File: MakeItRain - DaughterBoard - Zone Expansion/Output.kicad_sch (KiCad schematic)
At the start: 8 parts, among them P4 Screw_Terminal_01x02, Q7 2N7000, Q8 IRF9Z34NPBF

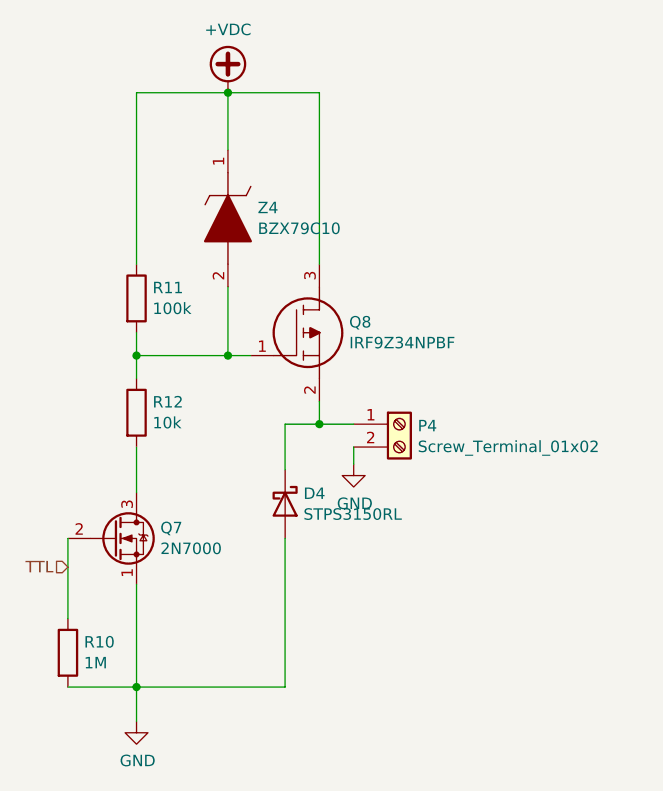
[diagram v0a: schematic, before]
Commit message: MakeItRain * Main Board Fixed Routing. * replaced Opamp with the part that i can get as the old one is EOL * generated all the fab files i need. * updated the daughter plug witht eh i2c ttl flip * fixed I2C issues * DRC'ed the board
MakeItRain - DaughterBoard - Zone Expansion
* updated the daughter plug witht eh i2c ttl flip
* fixed some of the routings
* generated new fab files
* DRC'ed the board
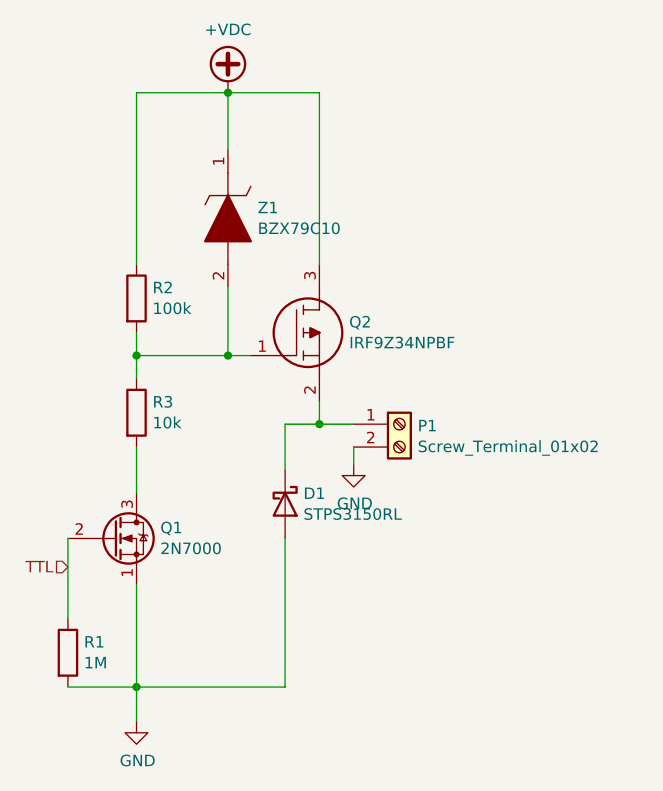
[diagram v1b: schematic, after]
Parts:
- renumbered D4 to D1, P4 to P1, Q7 to Q1, Q8 to Q2, R10 to R1, R11 to R2, R12 to R3, Z4 to Z1
